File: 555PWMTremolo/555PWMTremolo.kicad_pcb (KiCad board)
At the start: 2 copper layers, 54.6 x 98.6 mm, 41 parts

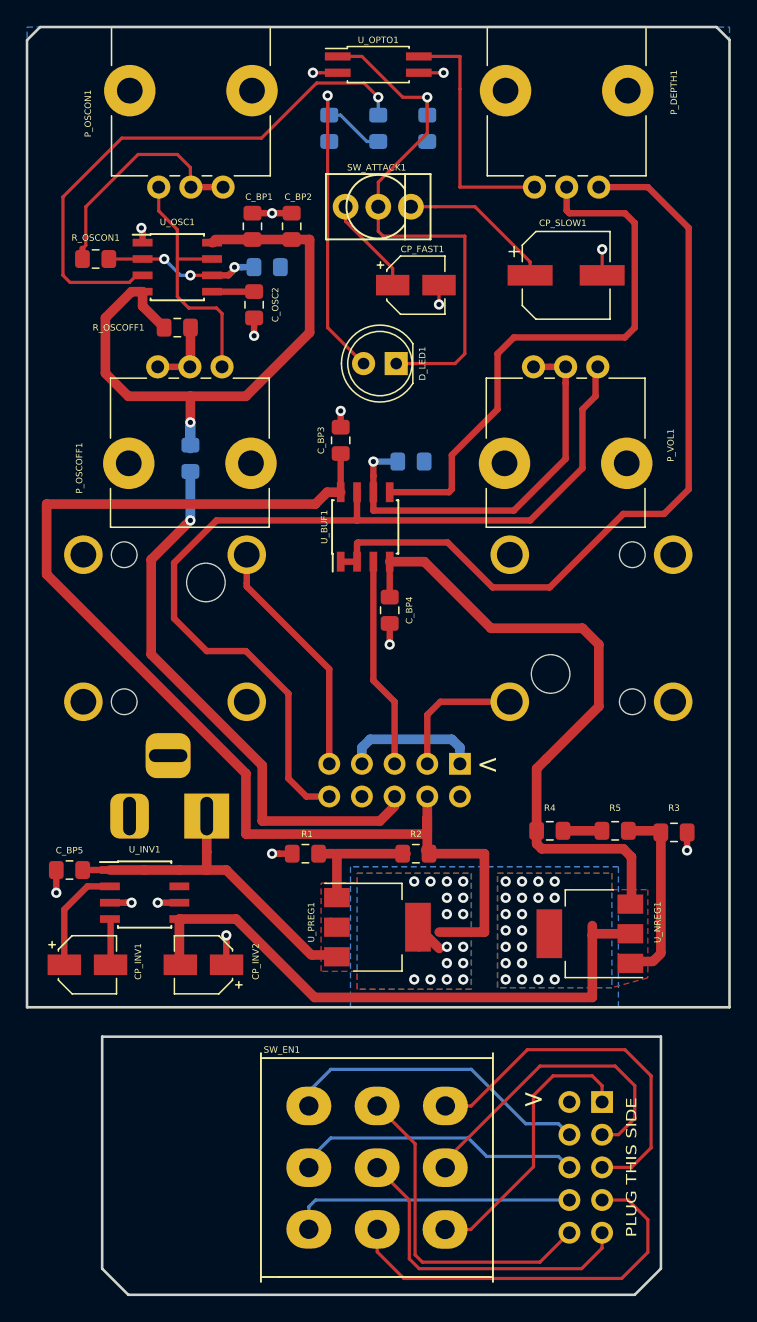
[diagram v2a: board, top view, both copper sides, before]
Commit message: Added second 555 IC bypass cap
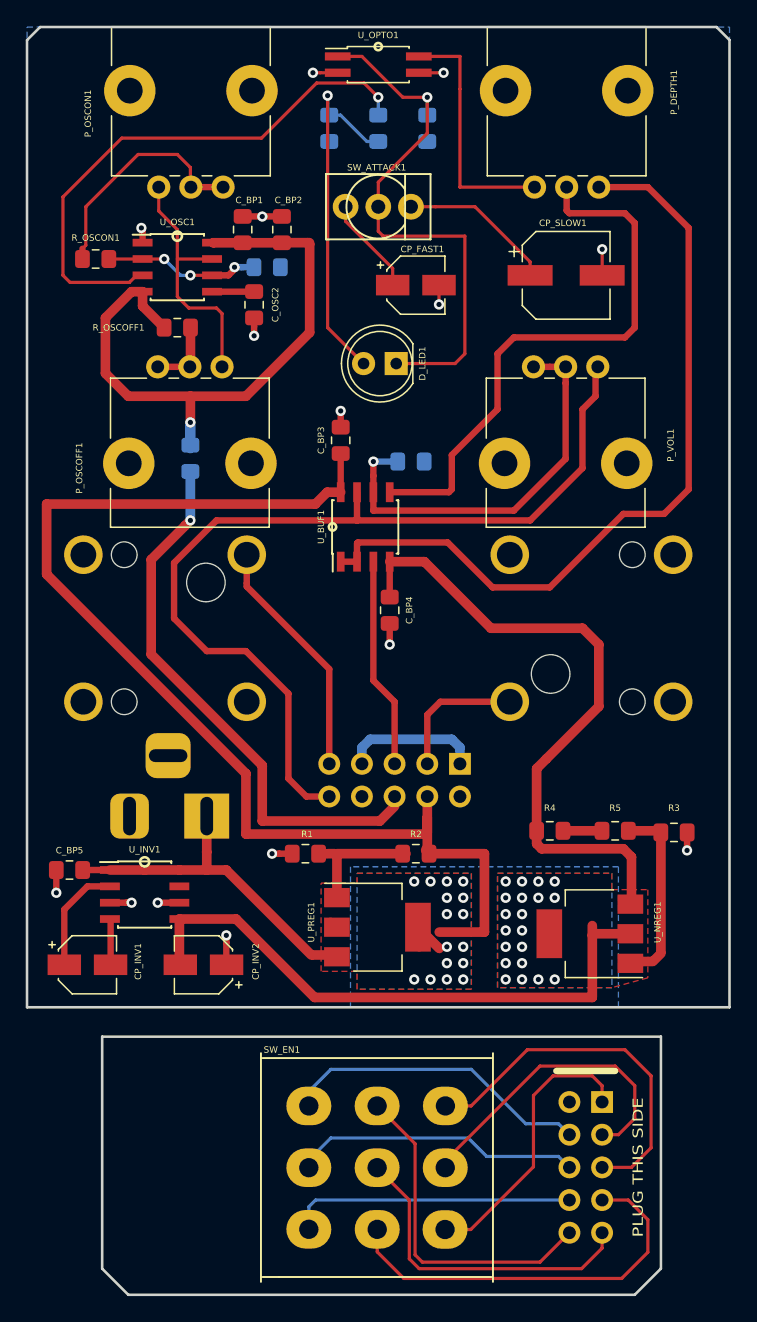
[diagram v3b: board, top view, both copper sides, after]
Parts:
- R_OSCOFF1, R_OSCON1: value 220R -> 1K
- moved C_BP1 0.80 mm to (70.1, 87.1)
- moved C_BP2 0.80 mm to (73.2, 87.1)
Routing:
- net Net-(C_BP1-Pad1): track 51.1 -> 50.3 mm
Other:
- board text added: "OPTO TREM Chris Sutton 2018 RevB"
- board text added: "OPTO TREM Chris Sutton RevB 2018"
- board text removed: ">"
- board text removed: "OPTO TREM Chris Sutton 2018 RevA"
- board text removed: "OPTO TREM Chris Sutton RevA 2018"
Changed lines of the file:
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@@
   (general
     (thickness 1.6)
-    (drawings 27)
-    (tracks 393)
+    (drawings 31)
+    (tracks 392)
     (zones 0)
     (modules 41)
@@
   )
   (setup
-    (last_trace_width 0.5)
+    (last_trace_width 0.25)
     (user_trace_width 0.5)
     (user_trace_width 0.75)
@@
     (descr "Through hole straight pin header, 2x05, 2.54mm pitch, double rows")
     (tags "Through hole pin header THT 2x05 2.54mm double row")
-    (fp_text reference J_AUXTOMAIN1 (at 1.27 2.33 180) (layer B.SilkS)
+    (fp_text reference J_AUXTOMAIN1 (at 1.27 -12.192 180) (layer B.SilkS)
       (effects (font (size 0.5 0.5) (thickness 0.125)) (justify mirror))
     )
@@
   )
   (module Capacitor_SMD:C_0805_2012Metric_Pad1.15x1.40mm_HandSolder (layer F.Cu)
-    (at 70.866 86.868 90)
+    (at 70.104 87.122 90)
     (descr "Capacitor SMD 0805 (2012 Metric), square (rectangular) end terminal, IPC_7351 nominal with elongated pad for handsoldering. (Body size source: https://docs.google.com/spreadsheets/d/1BsfQQcO9C6DZCsRaXUlFlo91Tg2WpOkGARC1WS5S8t0/edit?usp=sharing), generated with kicad-footprint-generator")
     (tags "capacitor handsolder")
@@
     (tags "SOIC 1.27")
     (attr smd)
-    (fp_text reference U_BUF1 (at 0 -3.175 270) (layer F.SilkS)
+    (fp_text reference U_BUF1 (at 0 -3.429 270) (layer F.SilkS)
       (effects (font (size 0.5 0.5) (thickness 0.125)))
     )
@@
       (effects (font (size 0.5 0.5) (thickness 0.125)))
     )
-    (fp_text value 220R (at 0 1.65 180) (layer F.Fab)
+    (fp_text value 1K (at 0 1.65 180) (layer F.Fab)
       (effects (font (size 0.5 0.5) (thickness 0.125)))
     )
@@
       (effects (font (size 0.5 0.5) (thickness 0.125)))
     )
-    (fp_text value 220R (at 0 1.65) (layer F.Fab)
+    (fp_text value 1K (at 0 1.65) (layer F.Fab)
       (effects (font (size 0.5 0.5) (thickness 0.125)))
     )
@@
     (tags "SO SOIC 1.27")
     (attr smd)
-    (fp_text reference U_OPTO1 (at 0 -1.905) (layer F.SilkS)
+    (fp_text reference U_OPTO1 (at 0 -2.286) (layer F.SilkS)
       (effects (font (size 0.5 0.5) (thickness 0.125)))
     )
@@
   )
   (module Capacitor_SMD:C_0805_2012Metric_Pad1.15x1.40mm_HandSolder (layer F.Cu)
-    (at 73.914 86.868 90)
+    (at 73.152 87.122 90)
     (descr "Capacitor SMD 0805 (2012 Metric), square (rectangular) end terminal, IPC_7351 nominal with elongated pad for handsoldering. (Body size source: https://docs.google.com/spreadsheets/d/1BsfQQcO9C6DZCsRaXUlFlo91Tg2WpOkGARC1WS5S8t0/edit?usp=sharing), generated with kicad-footprint-generator")
     (tags "capacitor handsolder")
@@
     )
   )
+  (gr_line (start 94.488 152.527) (end 99.06 152.527) (layer F.SilkS) (width 0.5))
+  (gr_line (start 89.535 127.889) (end 89.535 131.699) (layer B.SilkS) (width 0.5))
+  (gr_circle (center 62.484 136.271) (end 62.738 136.525) (layer F.SilkS) (width 0.2))
+  (gr_circle (center 77.089 110.236) (end 77.343 110.363) (layer F.SilkS) (width 0.2))
+  (gr_circle (center 80.645 72.898) (end 80.772 73.152) (layer F.SilkS) (width 0.2))
+  (gr_circle (center 65.024 87.63) (end 65.278 87.884) (layer F.SilkS) (width 0.2))
   (gr_text "higher val \nlower range" (at 71.882 87.122) (layer B.SilkS)
     (effects (font (size 0.8 0.8) (thickness 0.1)) (justify mirror))
@@
     (effects (font (size 0.6 0.6) (thickness 0.1)) (justify mirror))
   )
-  (gr_text > (at 89.154 128.778 180) (layer F.SilkS)
-    (effects (font (size 1.5 1.5) (thickness 0.3)))
-  )
-  (gr_text > (at 92.71 154.686) (layer F.SilkS)
-    (effects (font (size 1.5 1.5) (thickness 0.3)))
-  )
-  (gr_text "PLUG THIS SIDE" (at 100.33 160.02 90) (layer F.SilkS)
+  (gr_text "PLUG THIS SIDE" (at 100.838 160.02 90) (layer F.SilkS)
     (effects (font (size 0.8 1) (thickness 0.2)))
   )
@@
     (effects (font (size 0.8 1) (thickness 0.2)) (justify mirror))
   )
-  (gr_text "OPTO TREM\nChris Sutton\nRevA 2018" (at 99.187 131.191) (layer B.SilkS)
+  (gr_text "OPTO TREM\nChris Sutton\nRevB 2018" (at 99.187 131.191) (layer B.SilkS)
     (effects (font (size 1 1) (thickness 0.2)) (justify mirror))
   )
-  (gr_text "OPTO TREM\nChris Sutton\n2018 RevA" (at 65.532 159.766) (layer B.SilkS)
+  (gr_text "OPTO TREM\nChris Sutton\n2018 RevB" (at 65.532 159.766) (layer B.SilkS)
     (effects (font (size 1 1) (thickness 0.2)) (justify mirror))
   )
@@
   (via (at 70.993 95.377) (size 0.8) (drill 0.4) (layers F.Cu B.Cu) (net 36))
   (segment (start 70.993 94.664) (end 70.993 95.377) (width 0.5) (layer F.Cu) (net 36))
-  (via (at 72.39 85.852) (size 0.8) (drill 0.4) (layers F.Cu B.Cu) (net 36))
+  (via (at 71.628 86.106) (size 0.8) (drill 0.4) (layers F.Cu B.Cu) (net 36))
   (segment (start 77.724 102.48) (end 77.724 101.219) (width 0.5) (layer F.Cu) (net 36))
   (via (at 77.724 101.219) (size 0.8) (drill 0.4) (layers F.Cu B.Cu) (net 36))
@@
   (via (at 81.534 119.38) (size 0.8) (drill 0.4) (layers F.Cu B.Cu) (net 36))
   (segment (start 81.534 117.738) (end 81.534 119.38) (width 0.5) (layer F.Cu) (net 36))
-  (segment (start 70.866 85.843) (end 73.914 85.843) (width 0.5) (layer F.Cu) (net 36))
+  (segment (start 70.104 86.097) (end 73.152 86.097) (width 0.5) (layer F.Cu) (net 36))
   (segment (start 59.436 93.98) (end 59.436 98.298) (width 0.75) (layer F.Cu) (net 37))
   (segment (start 59.436 98.298) (end 61.214 100.076) (width 0.75) (layer F.Cu) (net 37))
@@
   (segment (start 62.324 93.067) (end 63.999 94.742) (width 0.75) (layer F.Cu) (net 37))
   (segment (start 62.324 91.948) (end 62.324 93.067) (width 0.75) (layer F.Cu) (net 37))
-  (segment (start 67.818 88.138) (end 67.724 88.138) (width 0.75) (layer F.Cu) (net 37))
+  (segment (start 67.827 88.147) (end 67.818 88.138) (width 0.75) (layer F.Cu) (net 37))
+  (segment (start 73.152 88.147) (end 67.827 88.147) (width 0.75) (layer F.Cu) (net 37))
+  (segment (start 73.406 88.138) (end 75.302 88.138) (width 0.75) (layer F.Cu) (net 37))
+  (segment (start 75.311 88.265) (end 75.184 88.138) (width 0.75) (layer F.Cu) (net 37))
+  (segment (start 75.311 95.123) (end 75.311 88.265) (width 0.75) (layer F.Cu) (net 37))
   (segment (start 70.358 100.076) (end 75.311 95.123) (width 0.75) (layer F.Cu) (net 37))
   (segment (start 66.04 100.076) (end 70.358 100.076) (width 0.75) (layer F.Cu) (net 37))
-  (segment (start 67.969 87.893) (end 67.724 88.138) (width 0.5) (layer F.Cu) (net 37))
-  (segment (start 73.914 87.893) (end 67.969 87.893) (width 0.75) (layer F.Cu) (net 37))
-  (segment (start 75.302 87.893) (end 75.311 87.884) (width 0.5) (layer F.Cu) (net 37))
-  (segment (start 73.914 87.893) (end 75.302 87.893) (width 0.75) (layer F.Cu) (net 37))
-  (segment (start 75.311 95.123) (end 75.311 87.884) (width 0.75) (layer F.Cu) (net 37))
   (via (at 84.455 76.835) (size 0.8) (drill 0.4) (layers F.Cu B.Cu) (net 38))
   (segment (start 84.455 76.835) (end 82.55 76.835) (width 0.25) (layer F.Cu) (net 38))

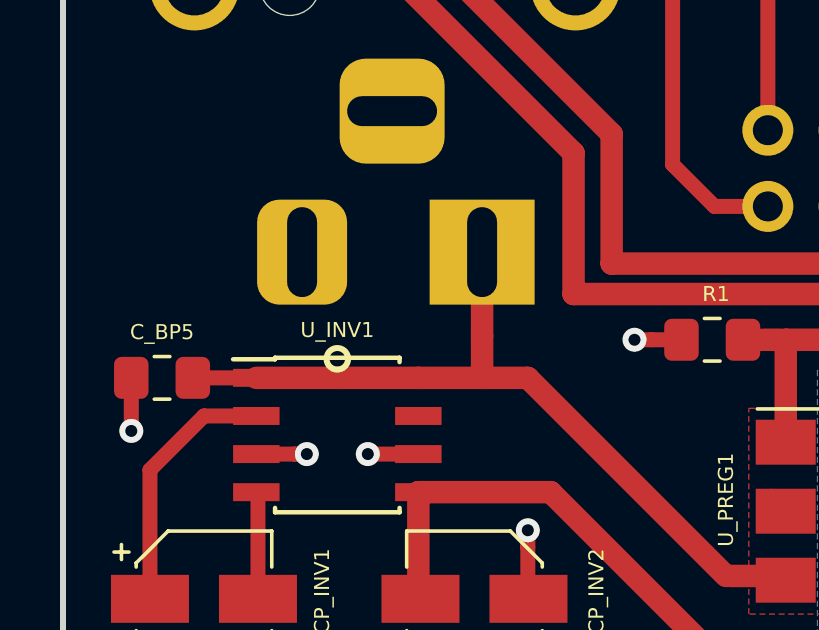
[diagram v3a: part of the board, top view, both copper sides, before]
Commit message: Corrected DC Jack polarity
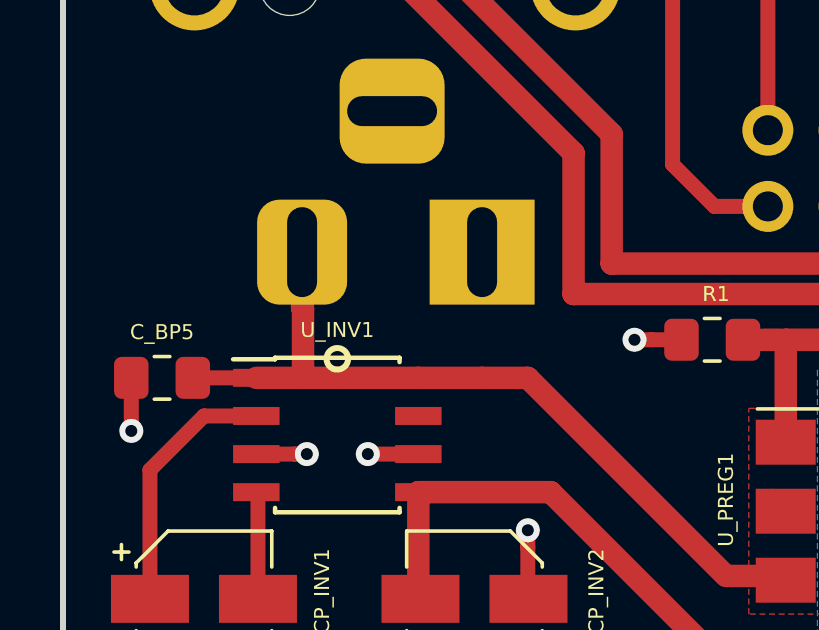
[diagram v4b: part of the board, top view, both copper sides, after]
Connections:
- J_PWR1 pad 1: +9V -> /GND
- J_PWR1 pad 2: /GND -> +9V
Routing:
- net +9V: track 25.7 -> 26.6 mm
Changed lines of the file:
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@@
     (thickness 1.6)
     (drawings 31)
-    (tracks 392)
+    (tracks 394)
     (zones 0)
     (modules 41)
@@
   )
   (setup
-    (last_trace_width 0.25)
+    (last_trace_width 0.75)
     (user_trace_width 0.5)
     (user_trace_width 0.75)
@@
     (fp_line (start 0 4.5) (end -13.7 4.5) (layer B.Fab) (width 0.1))
     (pad 1 thru_hole rect (at 0 0) (size 3.5 3.5) (drill oval 1 3) (layers *.Cu *.Mask)
+      (net 36 /GND))
+    (pad 2 thru_hole roundrect (at -6 0) (size 3 3.5) (drill oval 1 3) (layers *.Cu *.Mask) (roundrect_rratio 0.25)
       (net 5 +9V))
-    (pad 2 thru_hole roundrect (at -6 0) (size 3 3.5) (drill oval 1 3) (layers *.Cu *.Mask) (roundrect_rratio 0.25)
-      (net 36 /GND))
     (pad 3 thru_hole roundrect (at -3 -4.7) (size 3.5 3.5) (drill oval 3 1) (layers *.Cu *.Mask) (roundrect_rratio 0.25))
     (model ${KISYS3DMOD}/Connector_BarrelJack.3dshapes/BarrelJack_Horizontal.wrl
@@
   (segment (start 81.534 115.688) (end 81.534 112.936) (width 0.5) (layer F.Cu) (net 4))
   (segment (start 77.4175 143.637) (end 77.4315 143.651) (width 0.5) (layer F.Cu) (net 5) (status 30))
-  (segment (start 59.784 136.906) (end 62.484 136.906) (width 0.75) (layer F.Cu) (net 5))
   (segment (start 62.484 136.906) (end 65.184 136.906) (width 0.75) (layer F.Cu) (net 5))
-  (segment (start 67.31 135.509) (end 67.31 133.604) (width 0.75) (layer F.Cu) (net 5))
-  (segment (start 67.31 136.906) (end 67.31 135.509) (width 0.75) (layer F.Cu) (net 5))
   (segment (start 65.184 136.906) (end 67.31 136.906) (width 0.75) (layer F.Cu) (net 5))
   (segment (start 57.667 136.906) (end 59.784 136.906) (width 0.5) (layer F.Cu) (net 5))
@@
   (segment (start 68.834 136.906) (end 75.438 143.51) (width 0.75) (layer F.Cu) (net 5))
   (segment (start 67.31 136.906) (end 68.834 136.906) (width 0.75) (layer F.Cu) (net 5))
+  (segment (start 61.341 134.596) (end 61.341 136.906) (width 0.75) (layer F.Cu) (net 5))
+  (segment (start 61.31 134.565) (end 61.341 134.596) (width 0.75) (layer F.Cu) (net 5))
+  (segment (start 61.31 132.715) (end 61.31 134.565) (width 0.75) (layer F.Cu) (net 5))
+  (segment (start 61.341 136.906) (end 62.484 136.906) (width 0.75) (layer F.Cu) (net 5))
+  (segment (start 59.784 136.906) (end 61.341 136.906) (width 0.75) (layer F.Cu) (net 5))
   (segment (start 59.699 89.408) (end 62.324 89.408) (width 0.25) (layer F.Cu) (net 6) (status 30))
   (segment (start 62.324 89.408) (end 64.008 89.408) (width 0.25) (layer F.Cu) (net 6))
